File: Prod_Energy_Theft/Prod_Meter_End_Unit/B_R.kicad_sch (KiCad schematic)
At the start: 9 parts, among them Q1 BC817, Q2 BC817

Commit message: PCB
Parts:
- S1, S2: footprint USLPT2819DT2TR:SW_USLPT2819DT2TR -> theftdetection:SW_USLPT2819DT2TR
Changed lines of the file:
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@@
 			)
 		)
-		(property "Footprint" "USLPT2819DT2TR:SW_USLPT2819DT2TR"
+		(property "Footprint" "theftdetection:SW_USLPT2819DT2TR"
 			(at 154.94 62.23 0)
 			(effects
@@
 			)
 		)
-		(property "Footprint" "USLPT2819DT2TR:SW_USLPT2819DT2TR"
+		(property "Footprint" "theftdetection:SW_USLPT2819DT2TR"
 			(at 111.76 62.23 0)
 			(effects

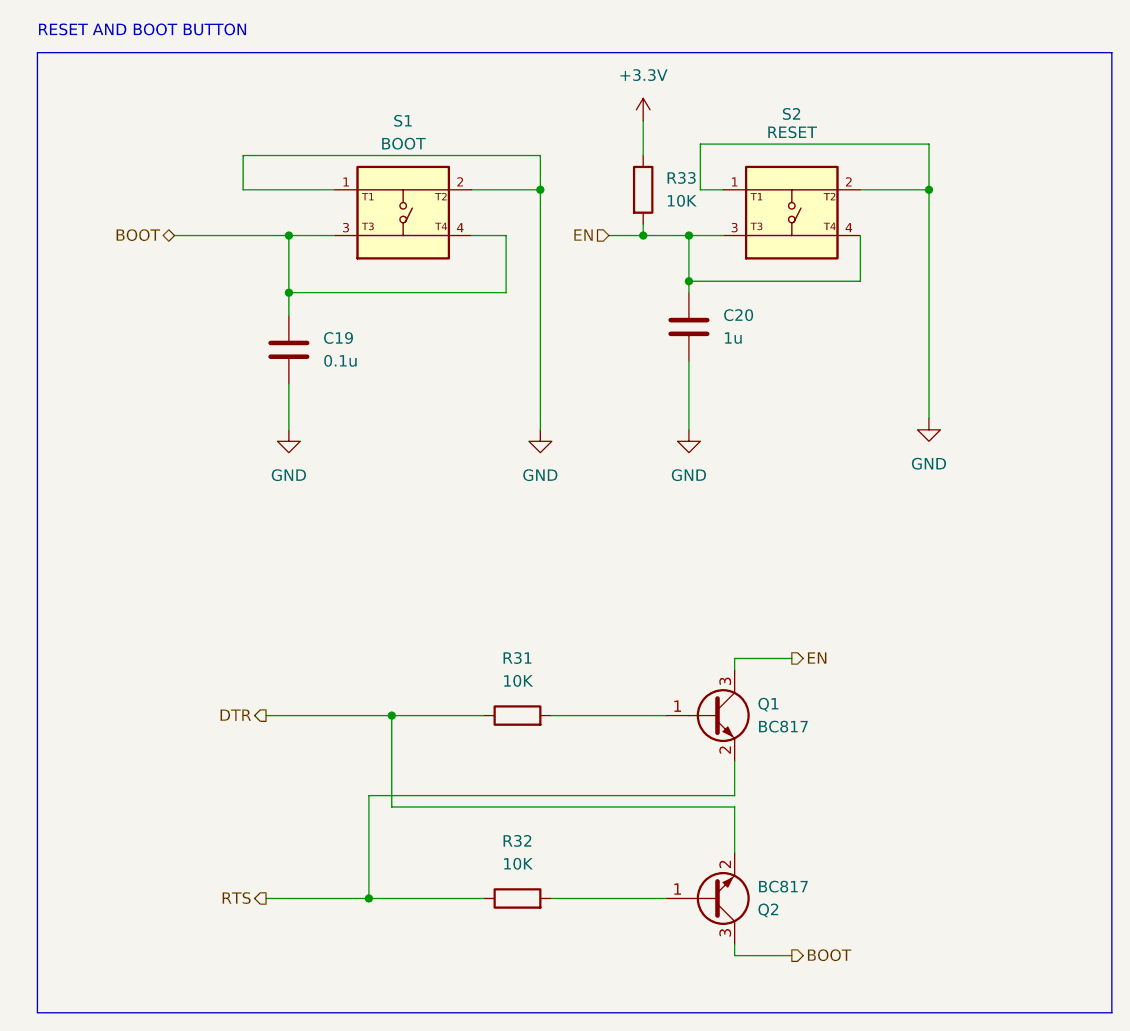
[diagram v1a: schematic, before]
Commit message: update in BOM list
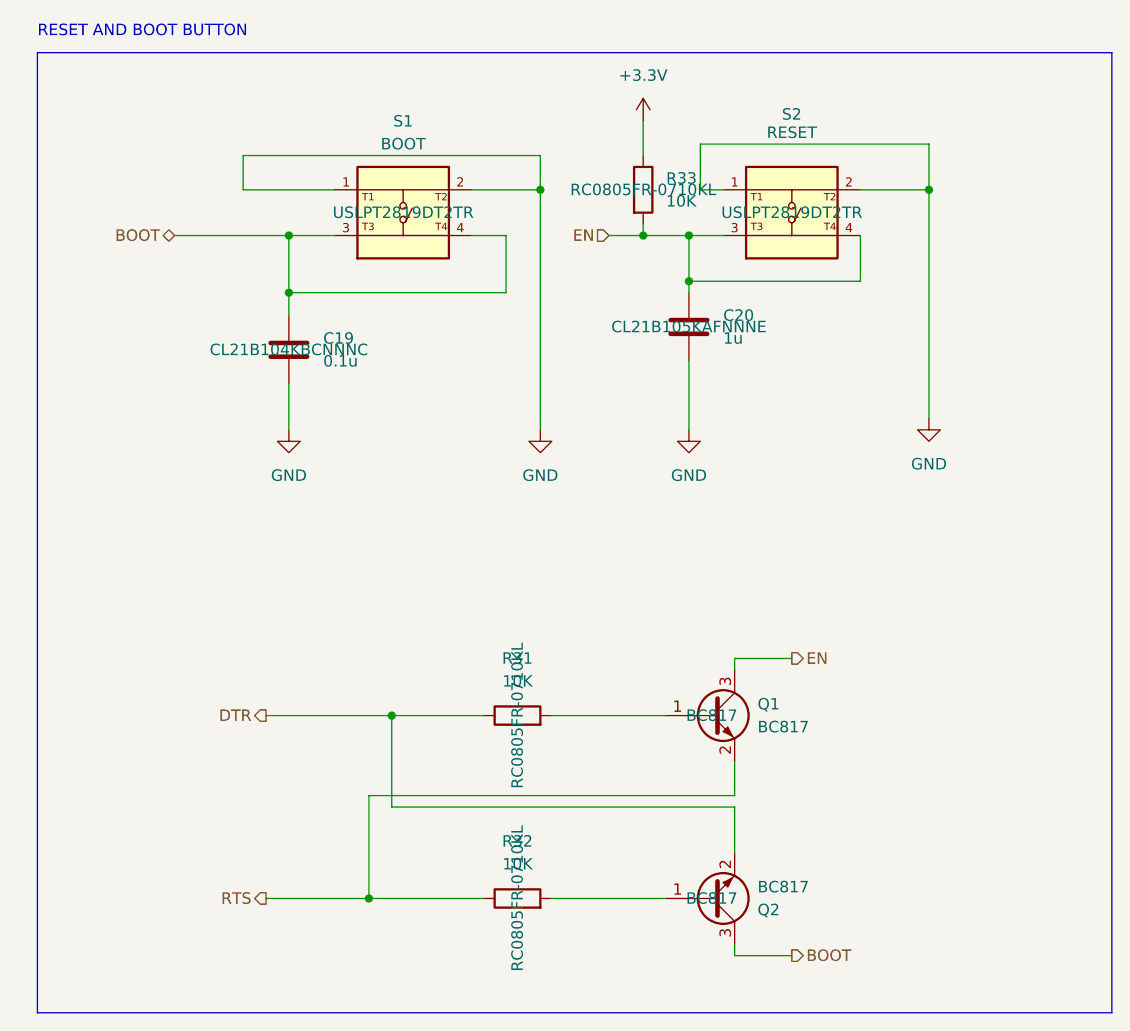
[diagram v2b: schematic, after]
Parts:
- C19: Part Number (none) -> CL21B104KBCNNNC
- C20: Part Number (none) -> CL21B105KAFNNNE
- Q1, Q2: Part Number (none) -> BC817
- R31, R32, R33: Part Number (none) -> RC0805FR-0710KL
- S1, S2: Part Number (none) -> USLPT2819DT2TR
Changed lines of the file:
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@@
+			)
+		)
+		(property "Part Number" "RC0805FR-0710KL "
+			(at 124.46 138.43 0)
+			(effects
+				(font
+					(size 1.27 1.27)
+				)
 			)
 		)
@@
 			)
 		)
+		(property "Part Number" "RC0805FR-0710KL "
+			(at 138.43 59.69 0)
+			(effects
+				(font
+					(size 1.27 1.27)
+				)
+			)
+		)
 		(pin "1"
 		)
@@
 			)
 		)
+		(property "Part Number" "BC817 "
+			(at 146.05 118.11 0)
+			(effects
+				(font
+					(size 1.27 1.27)
+				)
+			)
+		)
 		(pin "2"
 		)
@@
 			)
 		)
+		(property "Part Number" "CL21B104KBCNNNC "
+			(at 99.06 77.47 0)
+			(effects
+				(font
+					(size 1.27 1.27)
+				)
+			)
+		)
 		(pin "1"
 		)
@@
 			)
 		)
+		(property "Part Number" "RC0805FR-0710KL "
+			(at 124.46 118.11 0)
+			(effects
+				(font
+					(size 1.27 1.27)
+				)
+			)
+		)
 		(pin "2"
 		)
@@
 			)
 		)
+		(property "Part Number" "CL21B105KAFNNNE "
+			(at 143.51 74.93 0)
+			(effects
+				(font
+					(size 1.27 1.27)
+				)
+			)
+		)
 		(pin "1"
 		)
@@
 			)
 		)
+		(property "Part Number" "USLPT2819DT2TR "
+			(at 154.94 62.23 0)
+			(effects
+				(font
+					(size 1.27 1.27)
+				)
+			)
+		)
 		(pin "1"
 		)
@@
 			)
 		)
+		(property "Part Number" "BC817 "
+			(at 146.05 138.43 0)
+			(effects
+				(font
+					(size 1.27 1.27)
+				)
+			)
+		)
 		(pin "1"
 		)
@@
 			)
 		)
+		(property "Part Number" "USLPT2819DT2TR "
+			(at 111.76 62.23 0)
+			(effects
+				(font
+					(size 1.27 1.27)
+				)
+			)
+		)
